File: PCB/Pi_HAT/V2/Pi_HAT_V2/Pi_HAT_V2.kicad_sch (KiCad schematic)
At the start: 10 parts, among them J1 MPU9250, J2 Pi_GPIO, J3 Display

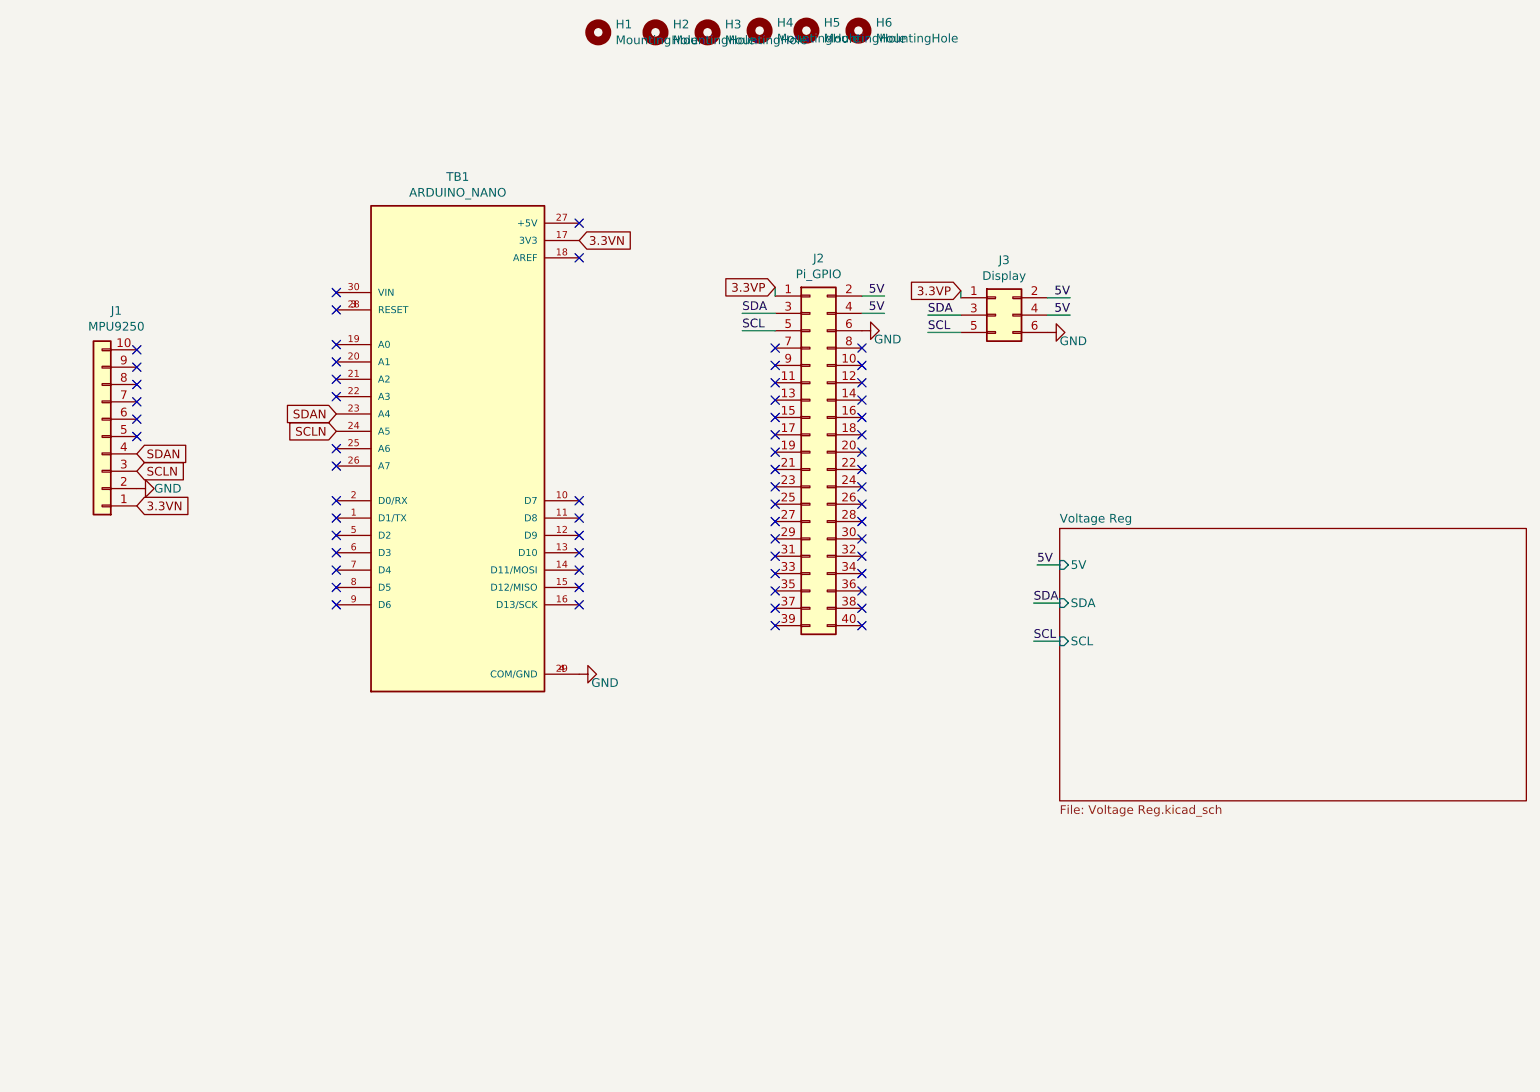
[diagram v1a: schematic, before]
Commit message: Finished Buch .sch
Next need to start/finish the PCB traces
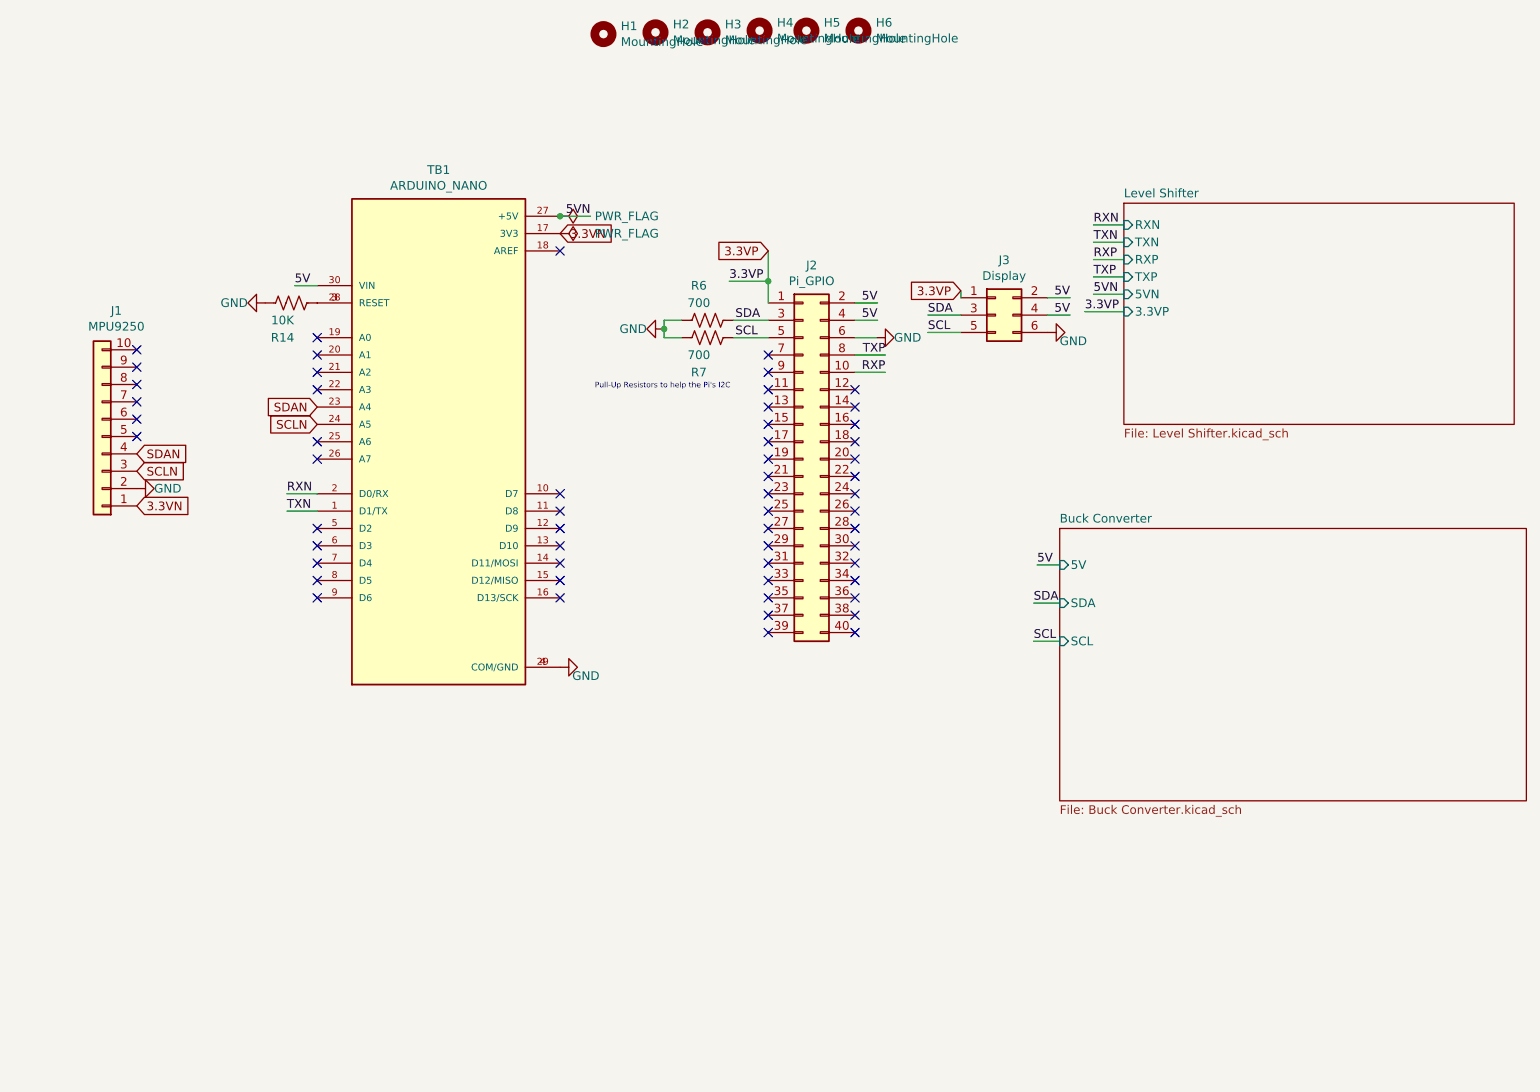
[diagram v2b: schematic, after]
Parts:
- added R14: 10K, Resistor_SMD:R_0805_2012Metric_Pad1.20x1.40mm_HandSolder, symbol Device:R_US
- added R6, R7: 700, Resistor_SMD:R_0603_1608Metric_Pad0.98x0.95mm_HandSolder, symbol Device:R_US
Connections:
- net 5V: now also TB1.30 (VIN)
- net GND: now also R14.1, R6.1, R7.1
- net SCL: now also R7.2
- net SDA: now also R6.2
- net TXN: now reaches TB1.1 (D1/TX)
- net RXN: now reaches TB1.2 (D0/RX)
- net 5VN: now reaches TB1.27 (+5V)
- net at TB1.28 (RESET), TB1.3 (RESET): now also R14.2
- net RXP: now reaches J2.10 (Pin_10)
- net TXP: now reaches J2.8 (Pin_8)
- no-connect marks 64 -> 57
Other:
- sheet Voltage Reg renamed Buck Converter
- added sheet Level Shifter (Level Shifter.kicad_sch)
- sheet Buck Converter: file Voltage Reg.kicad_sch -> Buck Converter.kicad_sch
- note added: "Pull-Up Resistors to help the Pi's I2C"
- moved on the sheet: H1, J2, TB1

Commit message: Updated
Added NANO_HAT and finished the PI_HAT V2 .sch, need to start/finish traces
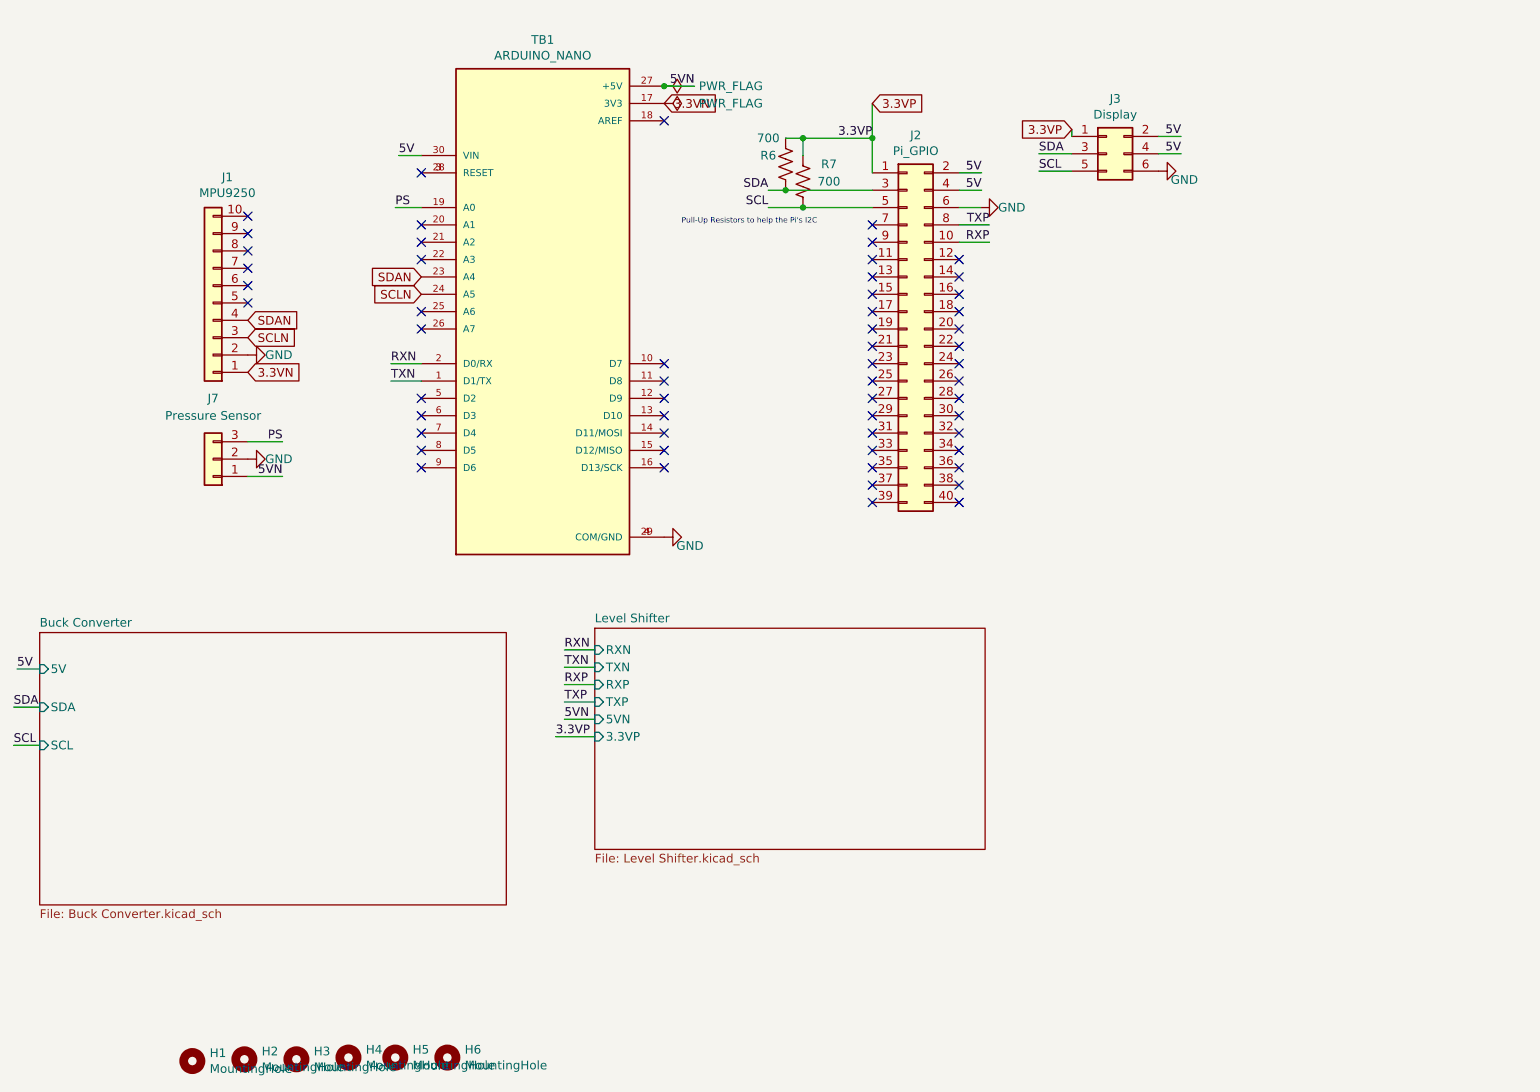
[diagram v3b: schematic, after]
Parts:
- removed R14: 10K, Resistor_SMD:R_0805_2012Metric_Pad1.20x1.40mm_HandSolder, symbol Device:R_US
- added J7: Pressure Sensor, Connector_PinHeader_2.54mm:PinHeader_1x03_P2.54mm_Vertical, symbol Connector_Generic:Conn_01x03
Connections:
- net 3.3VP: now also R6.2, R7.2
- net 5VN: now also J7.1 (Pin_1)
- net GND: now also J7.2 (Pin_2); no longer R6.1, R7.1
- net SCL: now also R7.1; no longer R7.2
- net SDA: now also R6.1; no longer R6.2
- net PS: now reaches TB1.19 (A0)
- net PS: now also J7.3 (Pin_3)
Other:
- moved on the sheet: H1, H2, H3, H4, H5, H6, J1, J2, J3, R6, R7, TB1

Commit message: Finished Pi HAT V2
Double checked all 'new' PCB's and made gerbers for all along with a BOM.
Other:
- sheet Level Shifter ports: added 5V; removed none
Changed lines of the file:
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@@
+    (stroke (width 0) (type default) (color 0 0 0 0))
+  )
+  (wire (pts (xy 135.128 137.287) (xy 138.43 137.287))
     (stroke (width 0) (type default) (color 0 0 0 0))
   )
@@
   (label "5V" (at 224.282 49.276 180)
     (effects (font (size 1.27 1.27)) (justify right bottom))
+  )
+  (label "5V" (at 135.128 137.287 0)
+    (effects (font (size 1.27 1.27)) (justify left bottom))
   )
   (label "PS" (at 92.71 91.44 180)
@@
       (effects (font (size 1.27 1.27)) (justify left))
     )
+    (pin "5V" input (at 138.43 137.287 180)
+      (effects (font (size 1.27 1.27)) (justify left))
+    )
   )
   (sheet_instances
@@
       (reference "#FLG0102") (unit 1) (value "PWR_FLAG") (footprint "")
     )
-    (path "/63a9d60b-f770-4724-9334-8ff781e7943f/8431275c-20f8-44c5-b8de-e1d08fb94e8f"
-      (reference "#FLG0104") (unit 1) (value "PWR_FLAG") (footprint "")
-    )
     (path "/63a9d60b-f770-4724-9334-8ff781e7943f/83a9f679-e1f3-4593-8827-5f5e89d70eaf"
       (reference "#FLG0105") (unit 1) (value "PWR_FLAG") (footprint "")
@@
       (reference "#FLG0106") (unit 1) (value "PWR_FLAG") (footprint "")
     )
-    (path "/63a9d60b-f770-4724-9334-8ff781e7943f/a27307d7-447c-4510-ab4e-ed44439e7d3d"
-      (reference "#FLG0107") (unit 1) (value "PWR_FLAG") (footprint "")
-    )
-    (path "/63a9d60b-f770-4724-9334-8ff781e7943f/328bba90-c0b4-457d-9ad3-f7a1739bbc96"
-      (reference "#FLG0108") (unit 1) (value "PWR_FLAG") (footprint "")
-    )
     (path "/63a9d60b-f770-4724-9334-8ff781e7943f/41b69d10-3a30-44c0-8a1e-2551c565103a"
       (reference "#FLG0109") (unit 1) (value "PWR_FLAG") (footprint "")
@@
       (reference "#PWR0117") (unit 1) (value "GND") (footprint "")
     )
-    (path "/63a9d60b-f770-4724-9334-8ff781e7943f/8bead41d-a0dd-465c-8d91-7e99cf899bc2"
-      (reference "#PWR0118") (unit 1) (value "+5V") (footprint "")
-    )
     (path "/63a9d60b-f770-4724-9334-8ff781e7943f/5eb6664f-8581-4539-b963-8b7278e419e4"
       (reference "#PWR0119") (unit 1) (value "+3.3V") (footprint "")
@@
       (reference "#PWR0120") (unit 1) (value "VAA") (footprint "")
     )
-    (path "/63a9d60b-f770-4724-9334-8ff781e7943f/23a48c58-1851-4aad-ac78-f55a61c90386"
-      (reference "#PWR0121") (unit 1) (value "VCC") (footprint "")
-    )
-    (path "/63a9d60b-f770-4724-9334-8ff781e7943f/08e875d3-7a37-4d02-b69f-954a7faaf62f"
-      (reference "#PWR0122") (unit 1) (value "VDC") (footprint "")
-    )
     (path "/63a9d60b-f770-4724-9334-8ff781e7943f/09be4d2a-a85e-4fc7-bd33-64682429c4b4"
